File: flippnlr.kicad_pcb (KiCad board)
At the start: 2 copper layers, 102 x 128 mm, 90 parts, among them J1 Data In, J2 Data Out, J8 12V, U1 SN74HCS594, U10 TPL7407LA, U11 TPL7407LA, U12 SN74HCS365, U13 LD1117 3.3V, U2 SN74HCS594, U3 SN74HCS594, U4 SN74HCS594, U5 SN74HCS594, U6 TPL7407LA, U7 TPL7407LA, U8 TPL7407LA, U9 TPL7407LA

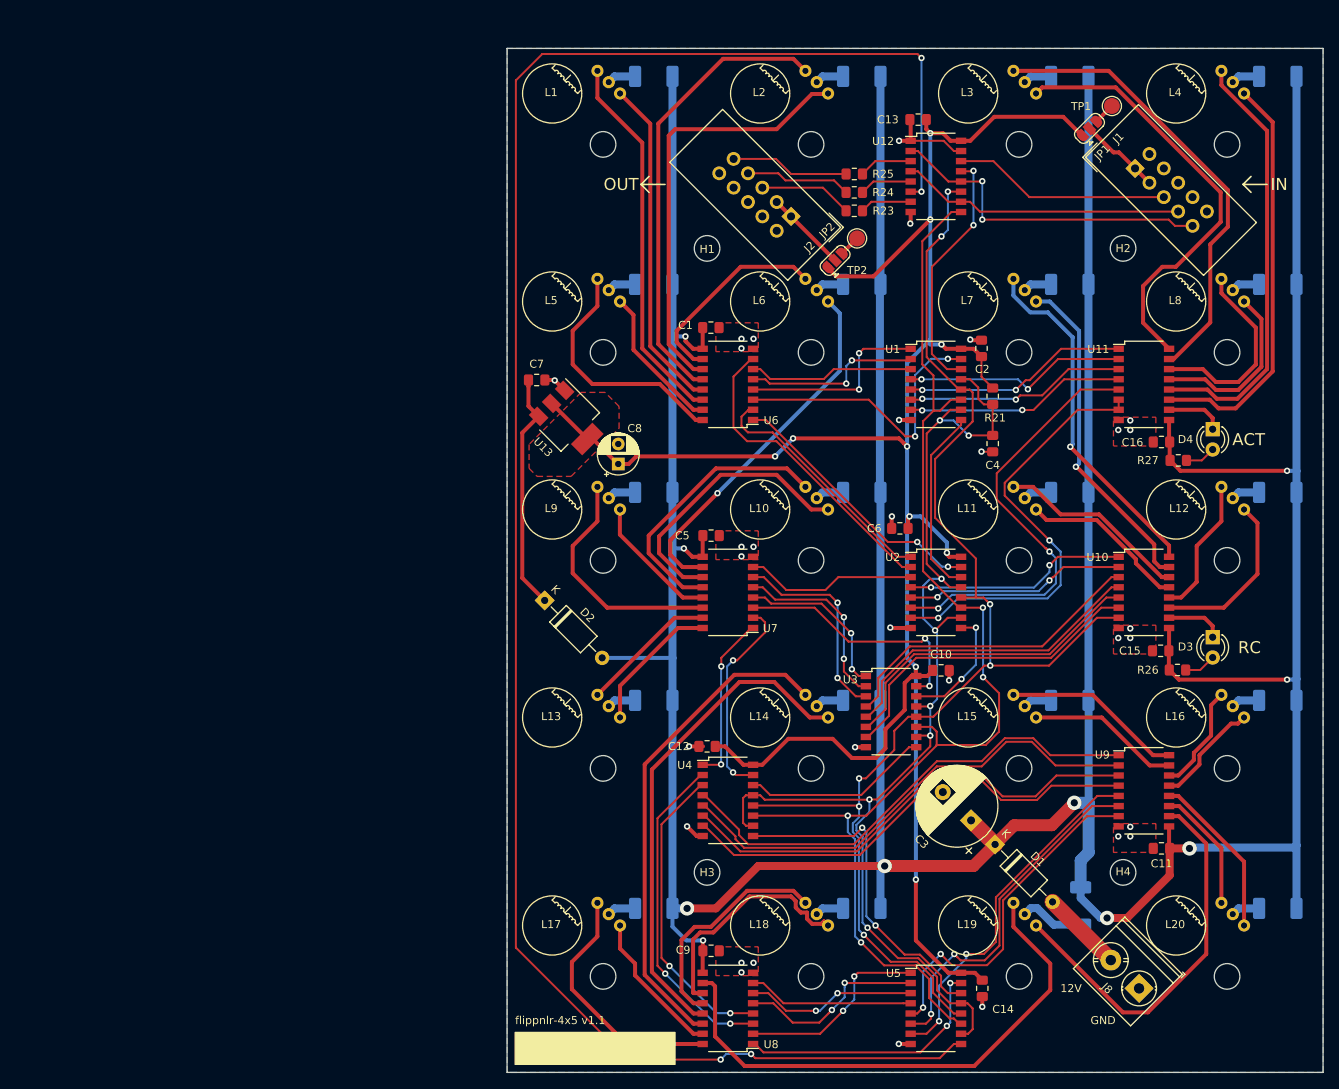
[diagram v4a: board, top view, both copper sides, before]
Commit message: correct Lx3/Lx7
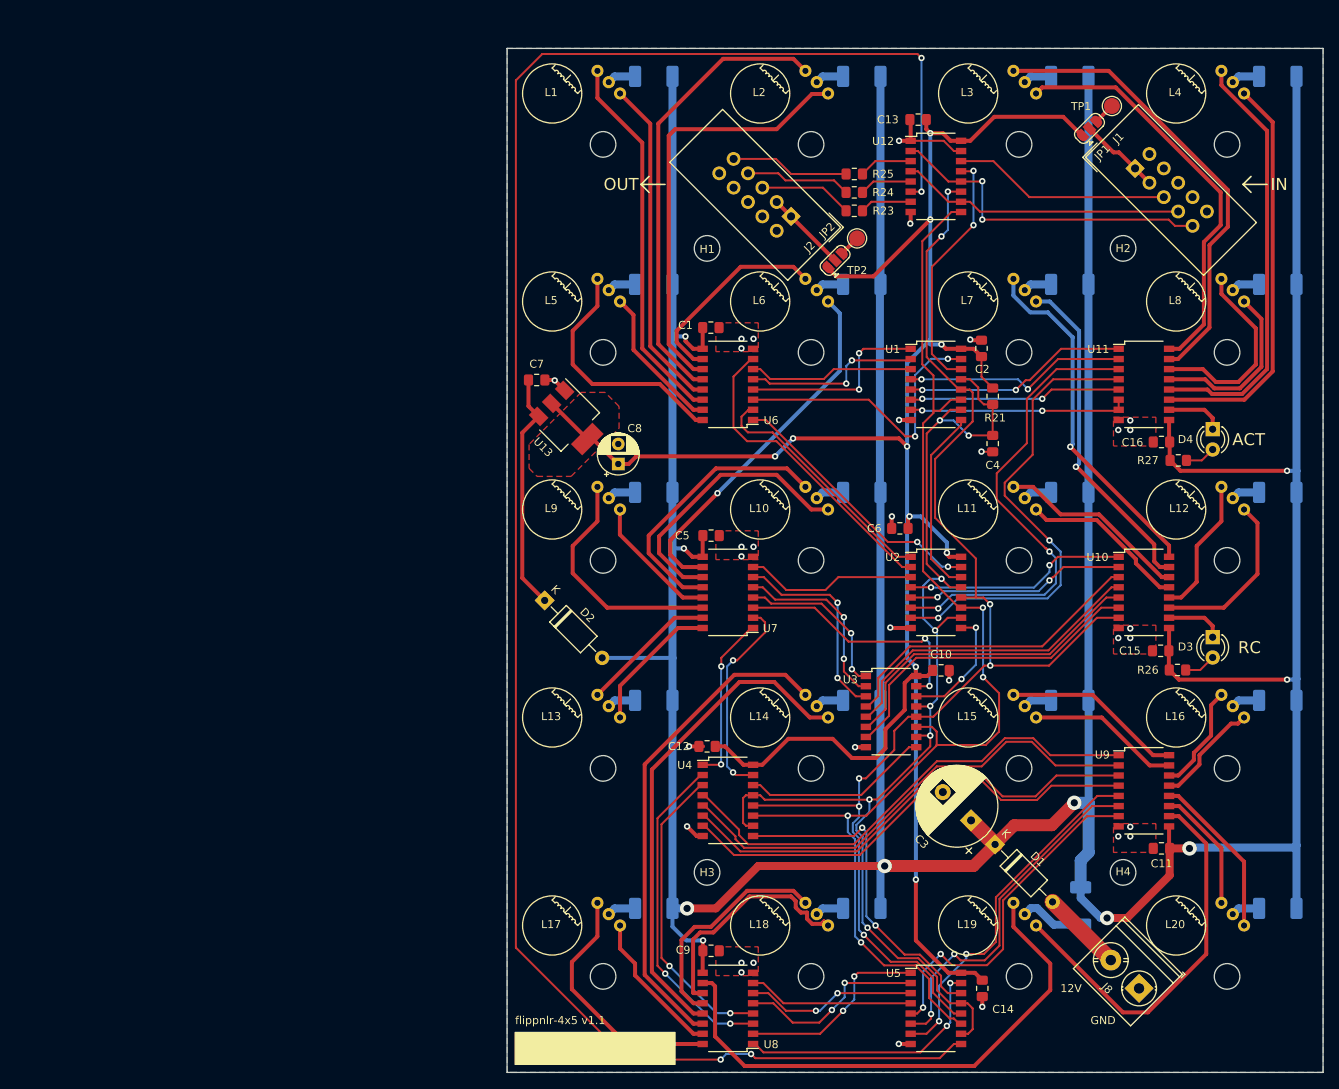
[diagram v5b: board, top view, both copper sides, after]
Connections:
- U11 pad 3: LS3 -> LS7
- U11 pad 4: LC3 -> LC7
- U11 pad 5: LS7 -> LS3
- U11 pad 6: LC7 -> LC3
- U11 pad 7: LC7 -> LC3
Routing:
- net LC7: track 55.4 -> 59.8 mm
- net LS7: track 55.9 -> 60.2 mm
- net C2: track 54.7 -> 51.8 mm
- net LS3: track 27.7 -> 26.5 mm
- net C3: track 51.5 -> 50.6 mm
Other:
- rule trace_min: 0.1524 -> 0.2
- rule via_min_size: 0.6858 -> 0.6

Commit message: prepare for gerbers
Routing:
- net S16: track 31.3 -> 23.8 mm
- net C17: track 29.7 -> 28.9 mm

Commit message: first prototype
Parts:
- R21: value 1k -> 4k7
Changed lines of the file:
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@@
       (effects (font (size 1 1) (thickness 0.15)))
     )
-    (fp_text value 1k (at 0 1.65 270) (layer F.Fab)
+    (fp_text value 4k7 (at 0 1.65 270) (layer F.Fab)
       (effects (font (size 1 1) (thickness 0.15)))
     )

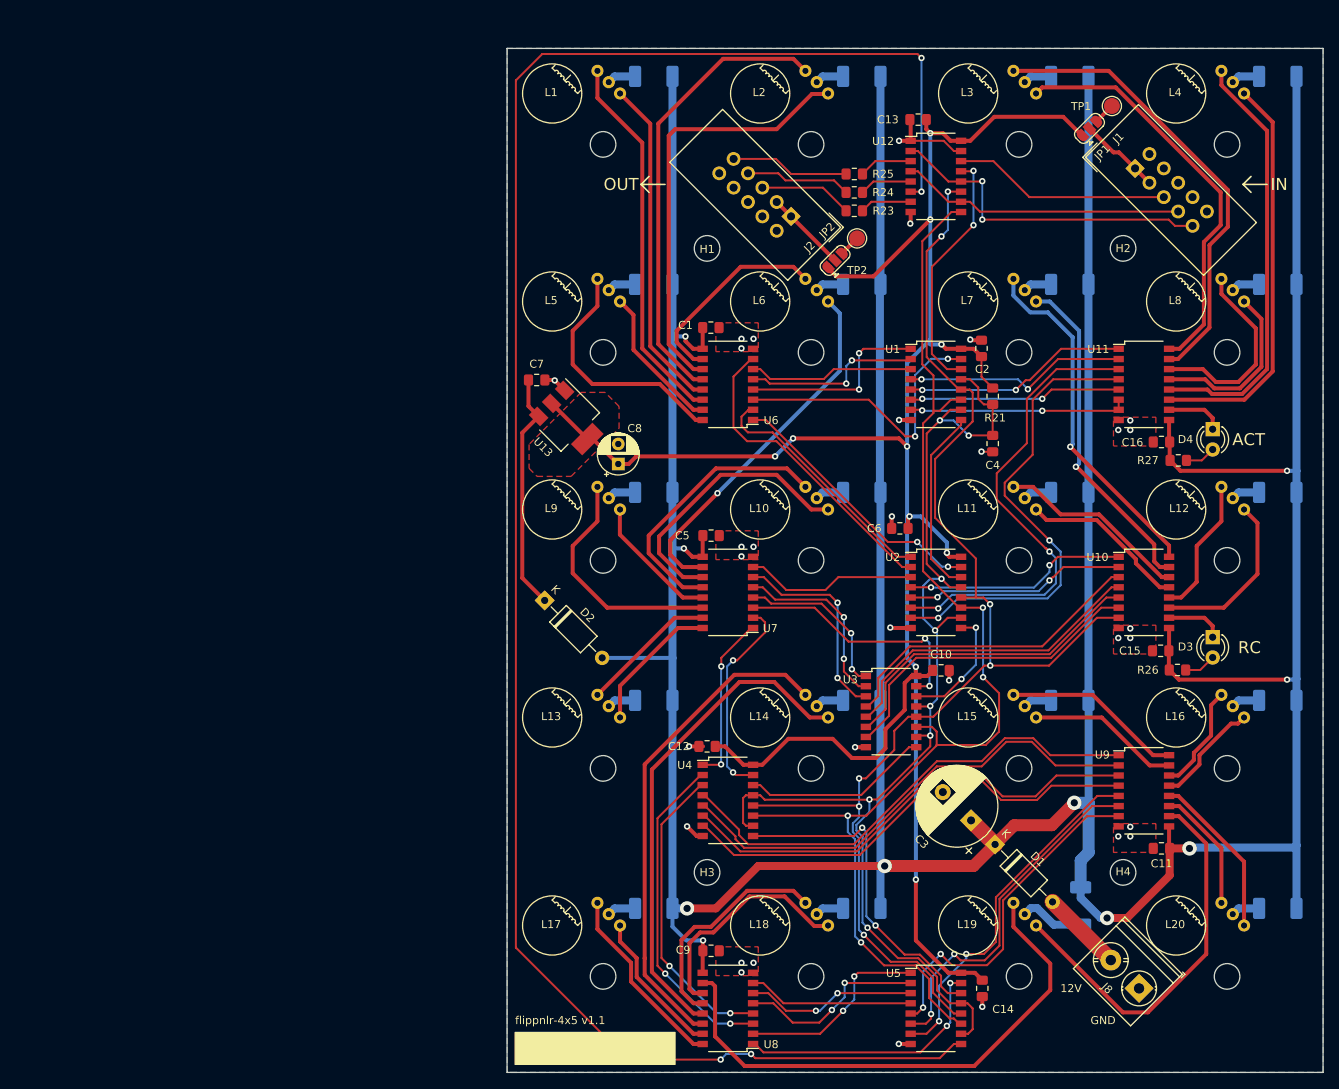
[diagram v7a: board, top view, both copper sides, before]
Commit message: Update to Kicad v6
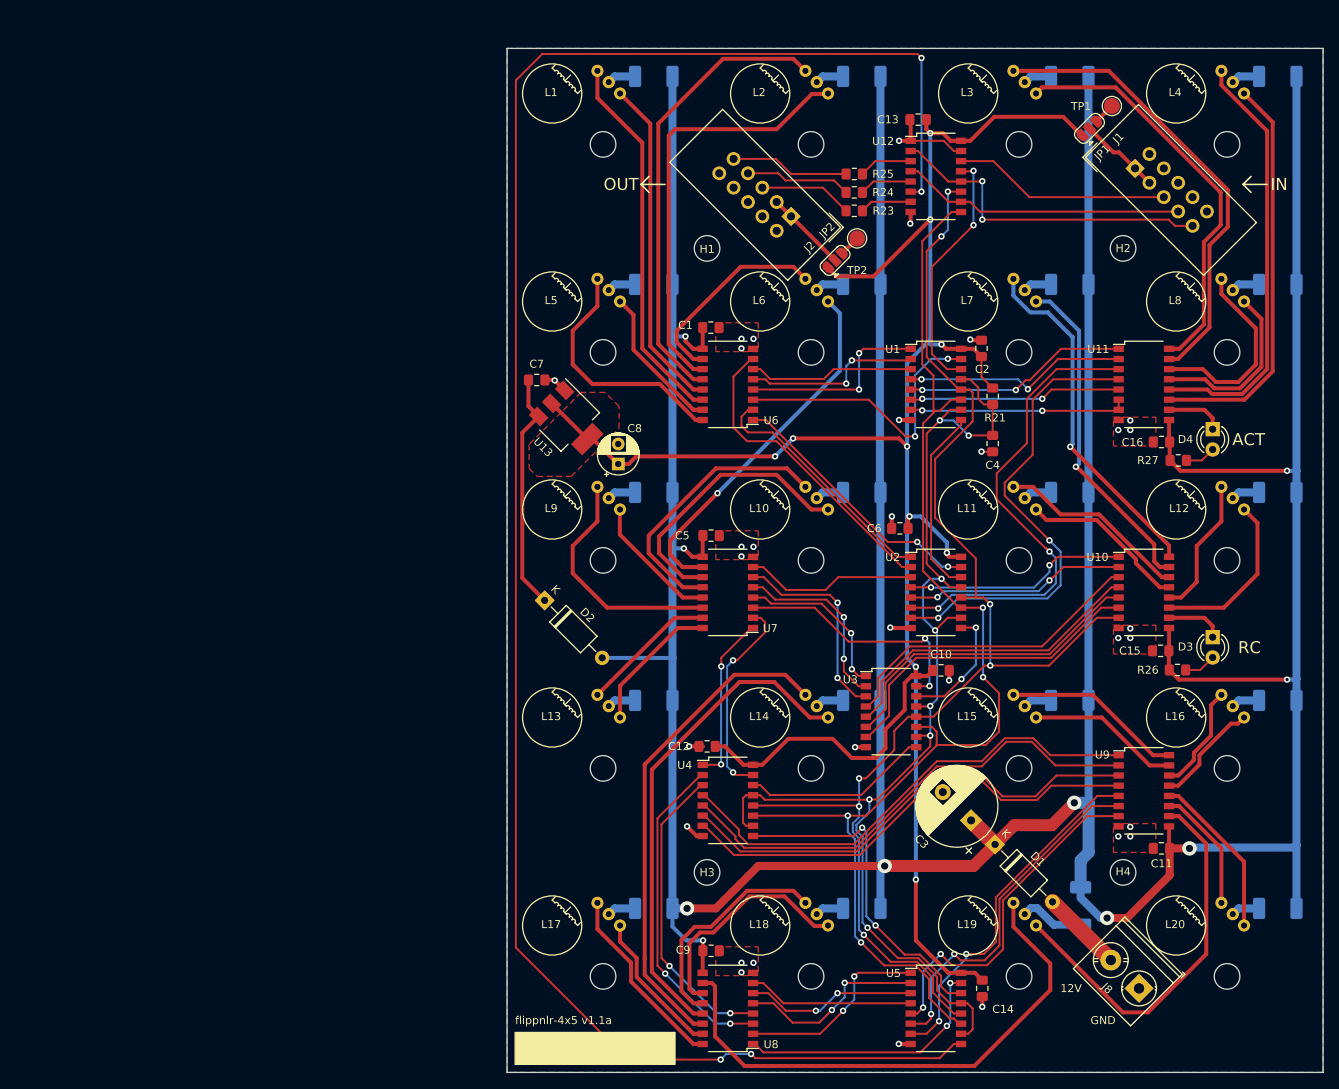
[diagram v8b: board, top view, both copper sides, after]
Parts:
- D1: value 1n5817 -> DNP
- R1, R10, R11, R12, R13, R14, R15, R16, R17, R18, R19, R2, R20, R3, R4, R5, R6, R7, R8, R9: value 62 -> 0R
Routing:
- net +3V3: track 265.5 -> 264.3 mm
- net +12V: track 590.8 -> 590.0 mm
- net RC: track 166.0 -> 165.3 mm
- net DC: track 152.7 -> 152.2 mm
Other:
- net class Default removed
- net class metrico removed
- board text added: "flippnlr-4x5 v1.1a"
- board text removed: "flippnlr-4x5 v1.1"
